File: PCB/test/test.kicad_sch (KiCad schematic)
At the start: 57 parts, among them U1 STM32WBxx_QFN48, U2 USBLC6-2SC6, U3 LD3985M33R, X1 NX2016_32MHz, X2 NX2012_32K768Hz

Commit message: ajout headers, reste circuit + UVNC
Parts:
- added HEADER1, HEADER2: 1-146285-0, TE_1-146285-0, symbol 1-146285-0:1-146285-0
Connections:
- net 3V3: now also HEADER1.9, HEADER2.9
- net 5V_USB: now also HEADER1.10, HEADER2.10
- net GND: now also HEADER1.1, HEADER2.1
- net PA0: now also HEADER1.8, HEADER2.8
- net PA1: now also HEADER1.7, HEADER2.7
- net PA2: now also HEADER1.6, HEADER2.6
- net PA3: now also HEADER1.5, HEADER2.5
- net PA4: now also HEADER1.4, HEADER2.4
- net PA5: now also HEADER1.3, HEADER2.3
- no-connect marks 14 -> 16

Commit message: filtres
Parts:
- added R10, R11: CRG0805ZR, RESC2012X65N, symbol CRG0805ZR:CRG0805ZR
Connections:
- net 3V3: now also BATTERY1.P1, BATTERY1.P2, HEADER1.10, HEADER2.10; no longer HEADER1.9, HEADER2.9
- net 5V_USB: no longer BATTERY1.P1, BATTERY1.P2, HEADER1.10, HEADER2.10
- net GND: now also R10.2, R11.2; no longer C41.1, C43.1, OXY1.1, OXY1.3, R4.1, R6.1, TSU1.13, TSU2.13
- net PA0: now also HEADER1.9, HEADER2.9, OXY1.6; no longer HEADER1.8, HEADER2.8, OXY1.9
- net PA1: now also HEADER1.8, HEADER2.8; no longer HEADER1.7, HEADER2.7
- net PA2: now also HEADER1.7, HEADER2.7, OXY1.9; no longer HEADER1.6, HEADER2.6, OXY1.6
- net PA3: now also HEADER1.6, HEADER2.6, OXY1.12; no longer C42.1, HEADER1.5, HEADER2.5, R5.2
- net PA4: now also C42.1, HEADER1.5, HEADER2.5, R5.2; no longer HEADER1.4, HEADER2.4, OXY1.12
- net PA5: now also HEADER1.4, HEADER2.4; no longer HEADER1.3, HEADER2.3
- new net: C43.1, OXY1.3, R11.1, R6.1, TSU2.13
- new net: C41.1, OXY1.1, R10.1, R4.1, TSU1.13
- no-connect marks 16 -> 18
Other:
- moved on the sheet: BATTERY1

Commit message: nettoyage routes et gnd
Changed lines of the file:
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@@
     (stroke (width 0.254) (type default) (color 0 0 0 0))
   )
-  (wire (pts (xy 26.67 46.99) (xy 25.4 46.99))
-    (stroke (width 0) (type default) (color 0 0 0 0))
-  )
   (wire (pts (xy 91.44 133.35) (xy 78.74 133.35))
     (stroke (width 0.254) (type default) (color 0 0 0 0))
@@
     (stroke (width 0.254) (type default) (color 0 0 0 0))
   )
-  (wire (pts (xy 26.67 35.56) (xy 25.4 35.56))
-    (stroke (width 0) (type default) (color 0 0 0 0))
-  )
   (wire (pts (xy 31.75 190.5) (xy 31.75 196.85))
     (stroke (width 0) (type default) (color 0 0 0 0))
@@
   (symbol (lib_id "armory:USB_A_PLUG") (at 7.62 41.91 90) (unit 1)
     (in_bom yes) (on_board yes)
-    (property "Reference" "USB1" (id 0) (at 12.7 29.21 90)
+    (property "Reference" "USB1" (id 0) (at -5.08 36.83 90)
       (effects (font (size 1.524 1.524)))
     )
-    (property "Value" "USB_A_PLUG" (id 1) (at 16.51 31.75 90)
+    (property "Value" "USB_A_PLUG" (id 1) (at -2.54 33.02 90)
       (effects (font (size 1.524 1.524)))
     )
@@
   (symbol (lib_id "test-altium-import:3V3") (at 49.53 88.9 180) (unit 1)
     (in_bom yes) (on_board yes)
-    (property "Reference" "#PWR?" (id 0) (at 49.53 88.9 0)
+    (property "Reference" "#PWR0167" (id 0) (at 49.53 88.9 0)
       (effects (font (size 1.27 1.27)) hide)
     )
@@
   (symbol (lib_id "test-altium-import:3V3") (at 21.59 59.69 180) (unit 1)
     (in_bom yes) (on_board yes)
-    (property "Reference" "#PWR?" (id 0) (at 21.59 59.69 0)
+    (property "Reference" "#PWR0169" (id 0) (at 21.59 59.69 0)
       (effects (font (size 1.27 1.27)) hide)
     )
@@
   )
   (symbol (lib_id "test-altium-import:5V_USB") (at 11.43 196.85 0) (unit 1)
-    (in_bom yes) (on_board yes) (fields_autoplaced)
+    (in_bom yes) (on_board yes)
     (property "Reference" "#PWR0150" (id 0) (at 11.43 191.77 0))
-    (property "Value" "5V_USB" (id 1) (at 11.43 194.31 0))
+    (property "Value" "5V_USB" (id 1) (at 11.43 201.93 0))
     (property "Footprint" "" (id 2) (at 11.43 196.85 0)
       (effects (font (size 1.27 1.27)) hide)
@@
     (pin "")
   )
-  (symbol (lib_id "test-altium-import:5V_USB") (at 26.67 46.99 90) (unit 1)
+  (symbol (lib_id "test-altium-import:5V_USB") (at 25.4 46.99 90) (unit 1)
     (in_bom yes) (on_board yes)
-    (property "Reference" "#PWR0161" (id 0) (at 26.67 46.99 0)
+    (property "Reference" "#PWR0161" (id 0) (at 25.4 46.99 0)
       (effects (font (size 1.27 1.27)) hide)
     )
-    (property "Value" "5V_USB" (id 1) (at 30.48 46.99 0))
-    (property "Footprint" "" (id 2) (at 26.67 46.99 0)
+    (property "Value" "5V_USB" (id 1) (at 29.21 46.99 0))
+    (property "Footprint" "" (id 2) (at 25.4 46.99 0)
       (effects (font (size 1.27 1.27)) hide)
     )
-    (property "Datasheet" "" (id 3) (at 26.67 46.99 0)
+    (property "Datasheet" "" (id 3) (at 25.4 46.99 0)
       (effects (font (size 1.27 1.27)) hide)
     )
@@
   )
   (symbol (lib_id "test-altium-import:GND") (at 31.75 196.85 0) (unit 1)
-    (in_bom yes) (on_board yes) (fields_autoplaced)
+    (in_bom yes) (on_board yes)
     (property "Reference" "#PWR0147" (id 0) (at 31.75 191.77 0))
-    (property "Value" "GND" (id 1) (at 31.75 194.31 0))
+    (property "Value" "GND" (id 1) (at 31.75 201.93 0))
     (property "Footprint" "" (id 2) (at 31.75 196.85 0)
       (effects (font (size 1.27 1.27)) hide)
@@
   (symbol (lib_id "test-altium-import:GND") (at 72.39 92.71 180) (unit 1)
     (in_bom yes) (on_board yes)
-    (property "Reference" "#PWR?" (id 0) (at 72.39 92.71 0)
+    (property "Reference" "#PWR0165" (id 0) (at 72.39 92.71 0)
       (effects (font (size 1.27 1.27)) hide)
     )
@@
   )
   (symbol (lib_id "test-altium-import:3V3") (at 21.59 196.85 0) (unit 1)
-    (in_bom yes) (on_board yes) (fields_autoplaced)
+    (in_bom yes) (on_board yes)
     (property "Reference" "#PWR0149" (id 0) (at 21.59 191.77 0))
-    (property "Value" "3V3" (id 1) (at 21.59 194.31 0))
+    (property "Value" "3V3" (id 1) (at 21.59 201.93 0))
     (property "Footprint" "" (id 2) (at 21.59 196.85 0)
       (effects (font (size 1.27 1.27)) hide)
@@
   (symbol (lib_id "test-altium-import:3V3") (at 6.35 88.9 180) (unit 1)
     (in_bom yes) (on_board yes)
-    (property "Reference" "#PWR?" (id 0) (at 6.35 88.9 0)
+    (property "Reference" "#PWR0166" (id 0) (at 6.35 88.9 0)
       (effects (font (size 1.27 1.27)) hide)
     )
@@
     (pin "")
   )
-  (symbol (lib_id "test-altium-import:GND") (at 26.67 35.56 90) (unit 1)
+  (symbol (lib_id "test-altium-import:GND") (at 25.4 35.56 90) (unit 1)
     (in_bom yes) (on_board yes)
-    (property "Reference" "#PWR0160" (id 0) (at 26.67 35.56 0)
+    (property "Reference" "#PWR0160" (id 0) (at 25.4 35.56 0)
       (effects (font (size 1.27 1.27)) hide)
     )
-    (property "Value" "GND" (id 1) (at 30.48 35.56 90)
+    (property "Value" "GND" (id 1) (at 29.21 35.56 90)
       (effects (font (size 1.27 1.27)) (justify right))
     )
-    (property "Footprint" "" (id 2) (at 26.67 35.56 0)
+    (property "Footprint" "" (id 2) (at 25.4 35.56 0)
       (effects (font (size 1.27 1.27)) hide)
     )
-    (property "Datasheet" "" (id 3) (at 26.67 35.56 0)
+    (property "Datasheet" "" (id 3) (at 25.4 35.56 0)
       (effects (font (size 1.27 1.27)) hide)
     )
@@
   (symbol (lib_id "test-altium-import:GND") (at 29.21 92.71 180) (unit 1)
     (in_bom yes) (on_board yes)
-    (property "Reference" "#PWR?" (id 0) (at 29.21 92.71 0)
+    (property "Reference" "#PWR0168" (id 0) (at 29.21 92.71 0)
       (effects (font (size 1.27 1.27)) hide)
     )
@@
       (reference "#PWR0164") (unit 1) (value "GND") (footprint "")
     )
-    (path "/2f0edba2-7967-4e1a-9684-2711d3990287"
-      (reference "#PWR?") (unit 1) (value "3V3") (footprint "")
-    )
-    (path "/3015f54c-ceea-4066-95ff-876921ea69e7"
-      (reference "#PWR?") (unit 1) (value "3V3") (footprint "")
-    )
     (path "/5aceded0-0ada-40ed-b4c9-7e65bbf2e463"
-      (reference "#PWR?") (unit 1) (value "GND") (footprint "")
+      (reference "#PWR0165") (unit 1) (value "GND") (footprint "")
     )
     (path "/bb780a84-8258-4112-91b0-8ea2082e609b"
-      (reference "#PWR?") (unit 1) (value "3V3") (footprint "")
+      (reference "#PWR0166") (unit 1) (value "3V3") (footprint "")
+    )
+    (path "/2f0edba2-7967-4e1a-9684-2711d3990287"
+      (reference "#PWR0167") (unit 1) (value "3V3") (footprint "")
     )
     (path "/c5e57d74-629e-46c9-a088-929c521900b3"
-      (reference "#PWR?") (unit 1) (value "GND") (footprint "")
+      (reference "#PWR0168") (unit 1) (value "GND") (footprint "")
+    )
+    (path "/3015f54c-ceea-4066-95ff-876921ea69e7"
+      (reference "#PWR0169") (unit 1) (value "3V3") (footprint "")
     )
     (path "/a771f6c7-2ee2-4da7-9645-2d519d6f98d9"

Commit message: réduction taille
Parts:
- removed TSU2: TSU104IPT, SOP65P640X120-14N, symbol TSU104IPT:TSU104IPT
- added unit 3 of TSU1
- renumbered BUZZER1 to BZR1, CONNECTEUR_NRST1 to NRST1, FIXATION_ECRAN1 to SCREEN1
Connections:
- net 3V3: no longer JOYSTICK1.1, JOYSTICK1.2, JOYSTICK1.3
- net GND: now also JOYSTICK1.5, TSU1.10
- net PA0: now also HEADER1.7, HEADER2.7; no longer HEADER1.9, HEADER2.9
- net PA1: now also HEADER1.6, HEADER2.6; no longer HEADER1.8, HEADER2.8
- net PA2: now also HEADER1.5, HEADER2.5; no longer HEADER1.7, HEADER2.7
- net PA3: now also HEADER1.4, HEADER2.4; no longer HEADER1.6, HEADER2.6
- net PA4: now also HEADER1.3, HEADER2.3; no longer HEADER1.5, HEADER2.5
- net PA5: now also HEADER1.2, HEADER2.2; no longer HEADER1.4, HEADER2.4
- net PA8: now also JOYSTICK1.6; no longer JOYSTICK1.5
- net PA9: now also JOYSTICK1.3; no longer JOYSTICK1.6
- net at C43.2, R5.1, R6.2: now also TSU1.8
- net at C43.1, OXY1.3, R11.1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: now also TSU1.9
- net PA6: now reaches U1.15 (PA6)
- net PA6: now also JOYSTICK1.2
- net PA10: now reaches U1.36 (PA10)
- net PA10: now also JOYSTICK1.1
- no-connect marks 18 -> 16
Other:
- moved on the sheet: R10, R11

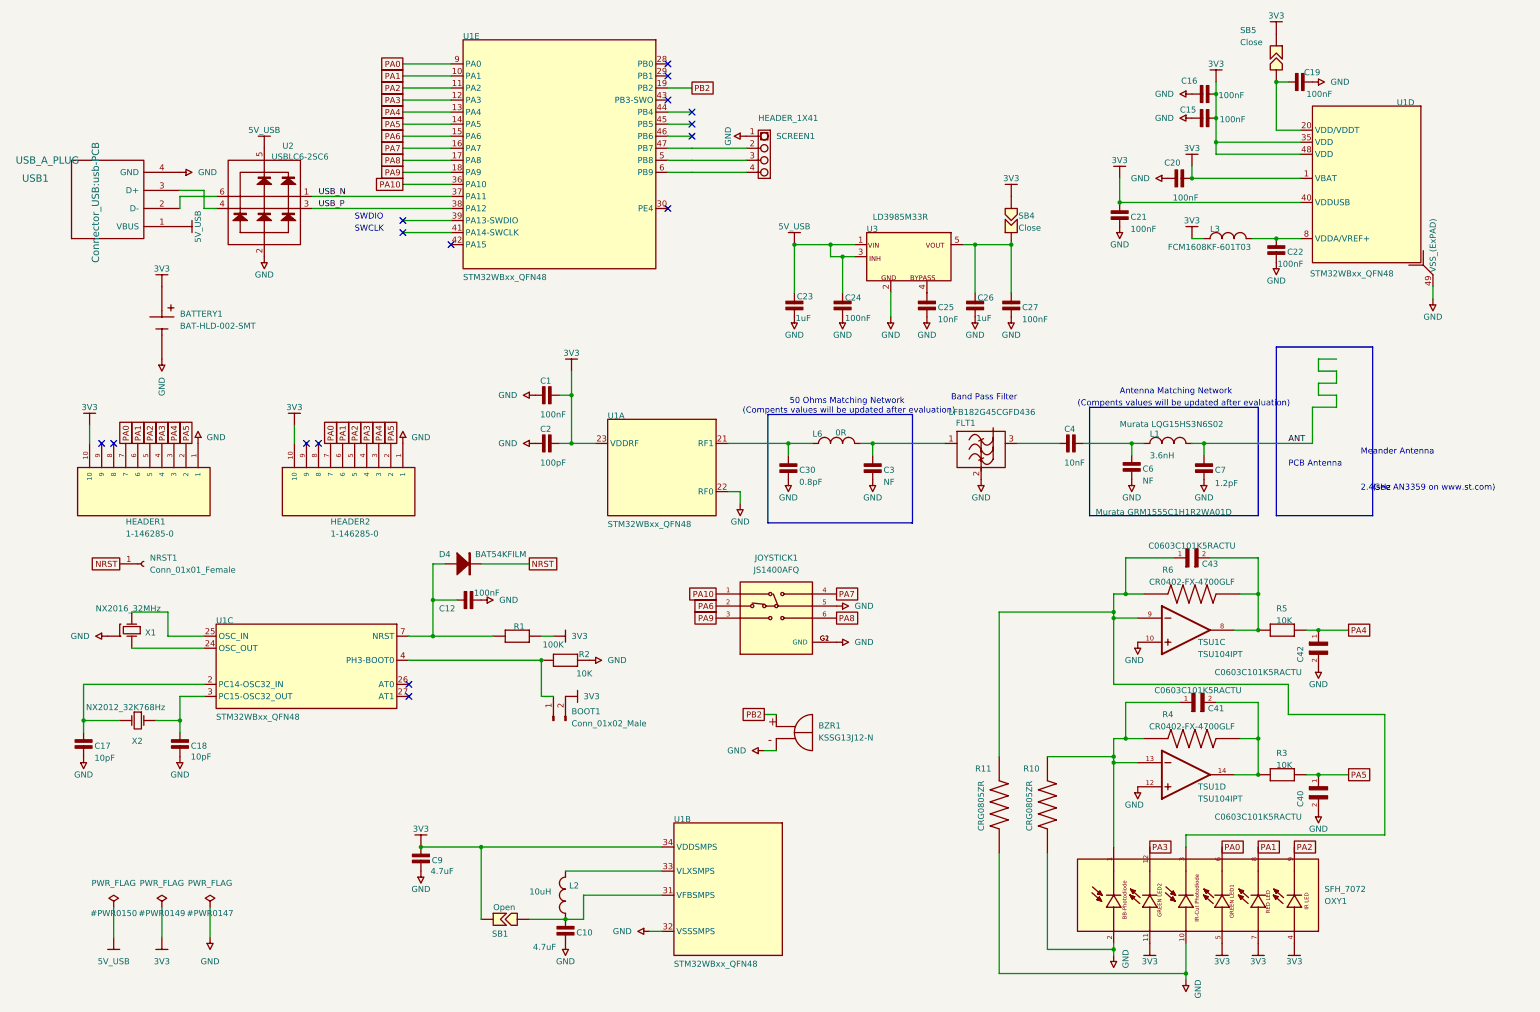
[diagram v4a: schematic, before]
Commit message: améliorations circuits, remplacement SFH7060 etc
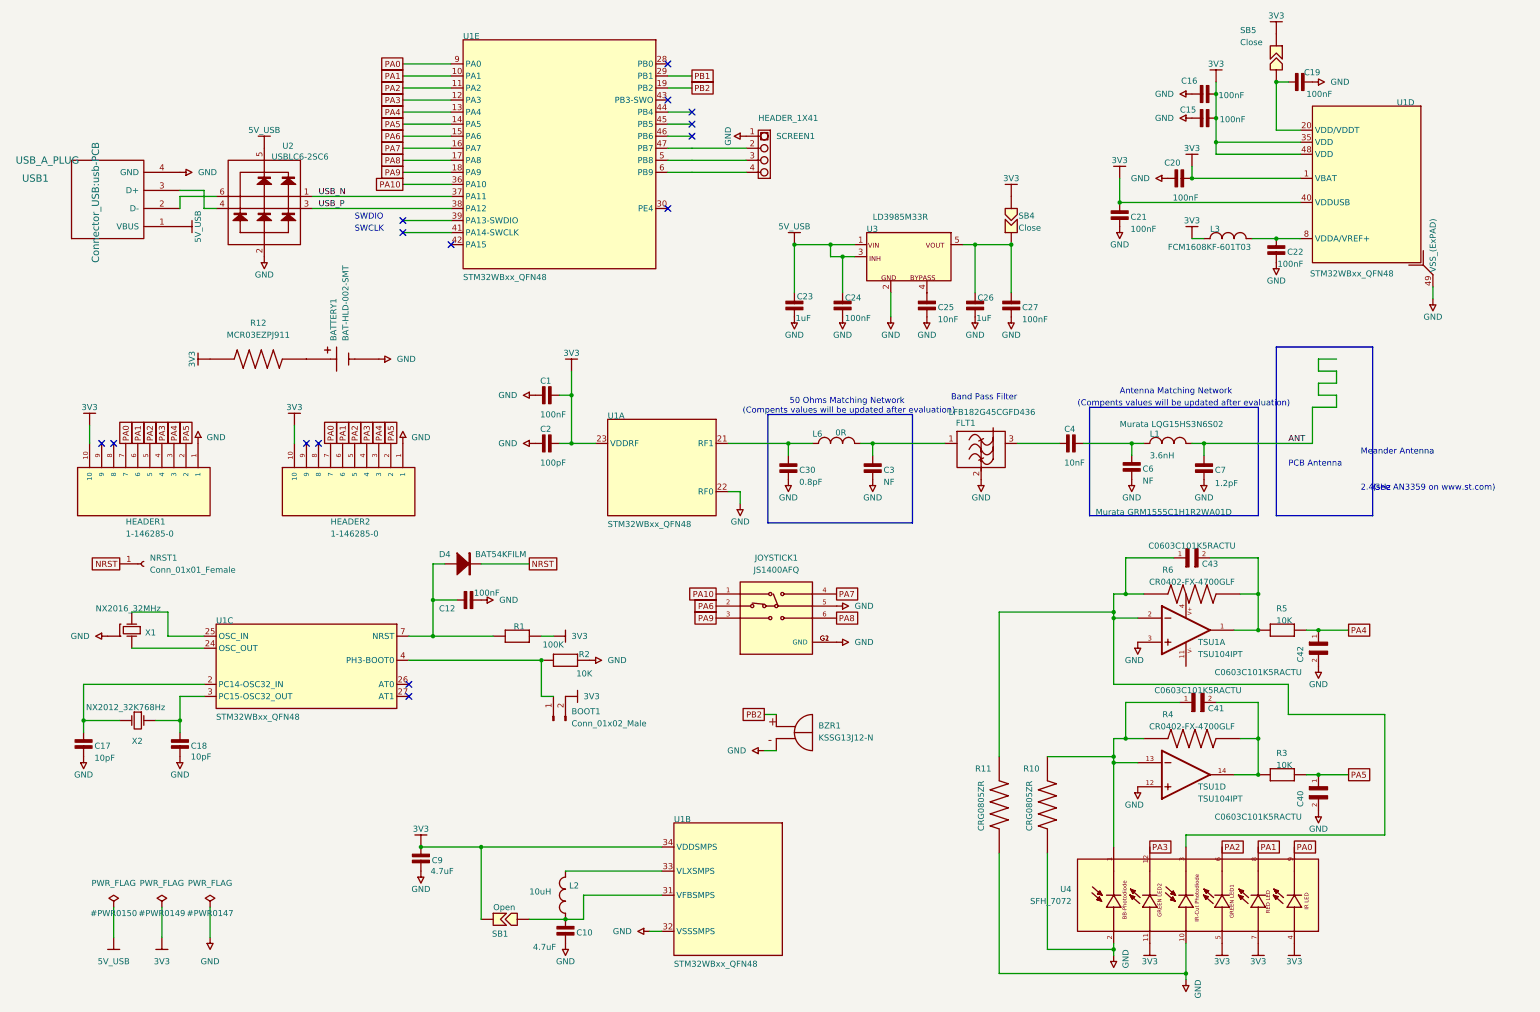
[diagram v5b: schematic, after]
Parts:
- removed OXY1: SFH_7072, XDCR_SFH_7060, symbol SFH_7072:SFH_7072
- added R12: MCR03EZPJ911, RESC1608X55N, symbol MCR03EZPJ911:MCR03EZPJ911
- added U4: SFH_7072, XDCR_SFH_7072, symbol SFH_7072:SFH_7072
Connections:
- net 3V3: now also R12.1, U4.11, U4.4, U4.5, U4.7; no longer BATTERY1.P1, BATTERY1.P2
- net GND: now also TSU1.3, U4.10, U4.2; no longer TSU1.10
- net PA0: now also U4.9
- net PA1: now also U4.8
- net PA2: now also U4.6
- net PA3: now also U4.12
- net at C43.2, R5.1, R6.2: now also TSU1.1; no longer TSU1.8
- net at C43.1, R11.1, R6.1: now also TSU1.2, U4.3; no longer TSU1.9
- net PB1: now reaches U1.29 (PB1)
- net at C41.1, R10.1, R4.1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: now also U4.1
- new net: BATTERY1.P1, BATTERY1.P2, R12.2
- no-connect marks 16 -> 15
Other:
- moved on the sheet: BATTERY1

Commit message: ajout pin monitoring pile
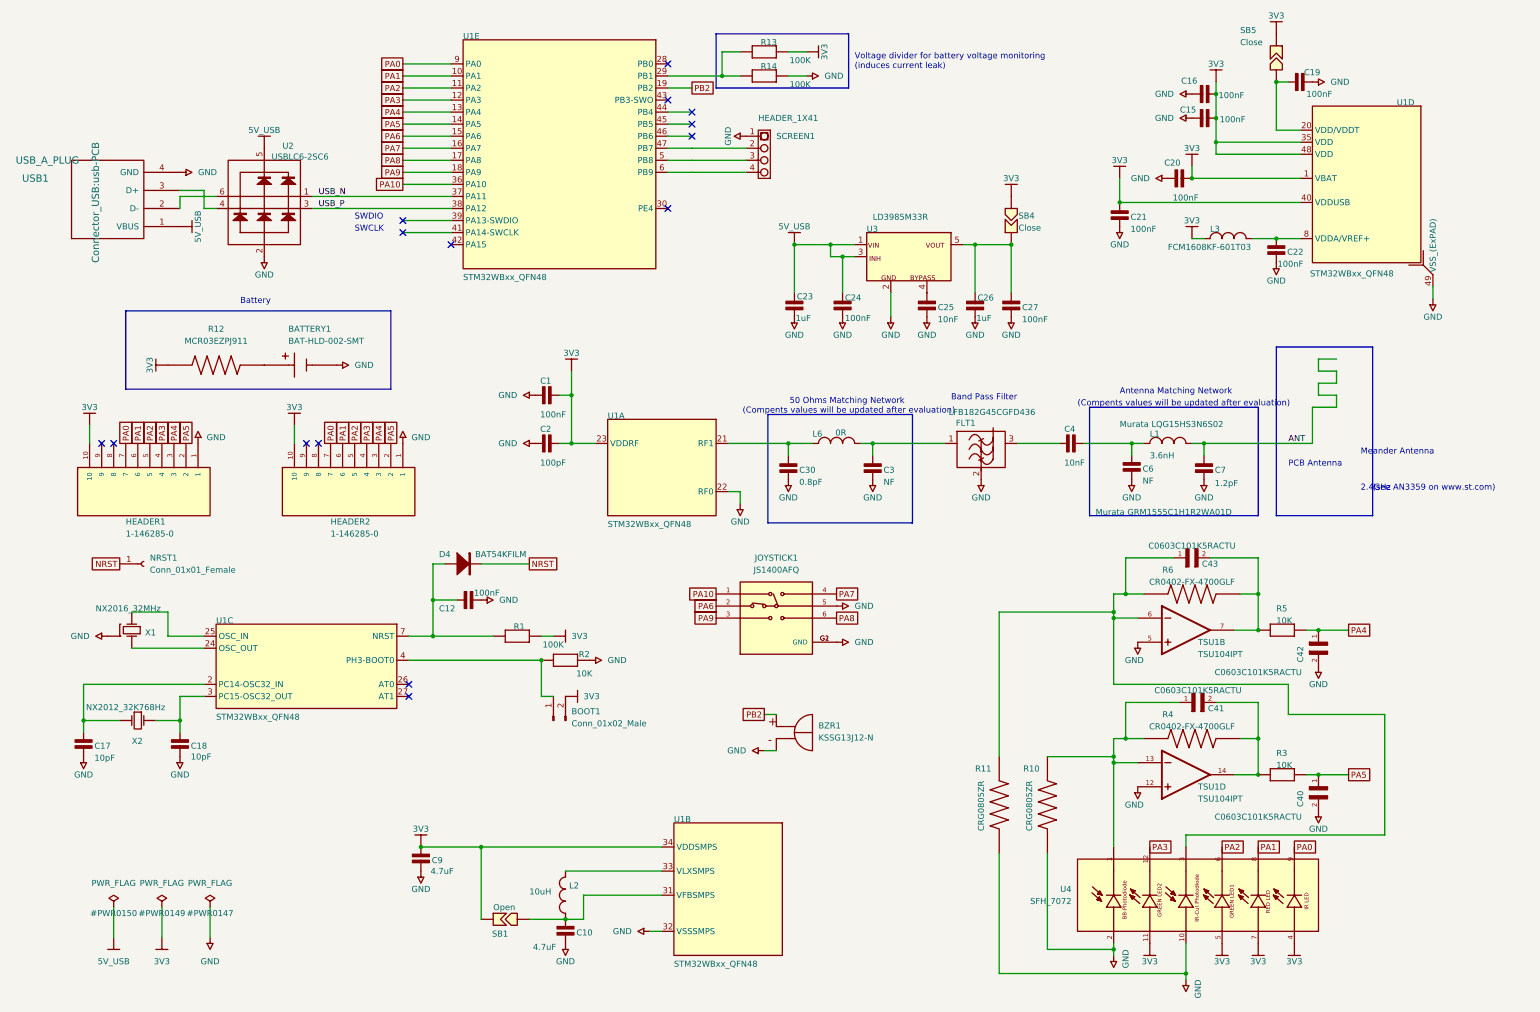
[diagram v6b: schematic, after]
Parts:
- added R13, R14: 100K, Library:0402_RES, symbol test-altium-import:2_RES
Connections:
- net 3V3: now also R13.1
- net GND: now also TSU1.5, R14.1; no longer TSU1.3
- net at C43.2, R5.1, R6.2: now also TSU1.7; no longer TSU1.1
- net at C43.1, R11.1, R6.1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: now also TSU1.6; no longer TSU1.2
- net PB1: no longer names the net of U1.29 (PB1)
- net PB1: now also R13.2, R14.2
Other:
- note added: "Battery"
- note added: "Voltage divider for battery voltage monitoring (induces current leak)"
- moved on the sheet: BATTERY1, R12

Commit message: ajout alim TSU104
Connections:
- net 3V3: now also TSU1.4
- net GND: now also TSU1.11, TSU1.3; no longer TSU1.5
- net at C43.2, R5.1, R6.2: now also TSU1.1; no longer TSU1.7
- net at C43.1, R11.1, R6.1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: now also TSU1.2; no longer TSU1.6
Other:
- moved on the sheet: C43, R6
